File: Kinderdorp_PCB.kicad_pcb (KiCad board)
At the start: 2 copper layers, 99.1 x 99.1 mm, 46 parts, among them Q1 2N7002_C306856, U1 AMS1117-3.3_C347222, U2 ESP32-C3-WROOM-02-N4(4MB)

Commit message: moved board to centre
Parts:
- moved BT1: 29.4 mm to (150.1, 90.6)
- moved D1 29.4 mm to (173.2, 127.0)
- moved G*** 29.4 mm to (169.6, 64.8)
- moved LED5 29.4 mm to (159.4, 56.6)
- moved BUTTON1 29.4 mm to (182.7, 99.9)
- moved C1 29.4 mm to (164.8, 127.5)
- moved C3 29.4 mm to (159.2, 141.4)
- moved F1 29.4 mm to (171.4, 133.2)
- moved GND 29.4 mm to (131.1, 116.0)
- moved LED3 29.4 mm to (102.8, 84.9)
- moved LED4 29.4 mm to (109.8, 57.5)
- moved LED8 29.4 mm to (151.8, 134.5)
- moved LS1 29.4 mm to (122.3, 81.5)
- moved R1 29.4 mm to (104.2, 122.1)
- moved R3 29.4 mm to (178.7, 124.8)
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
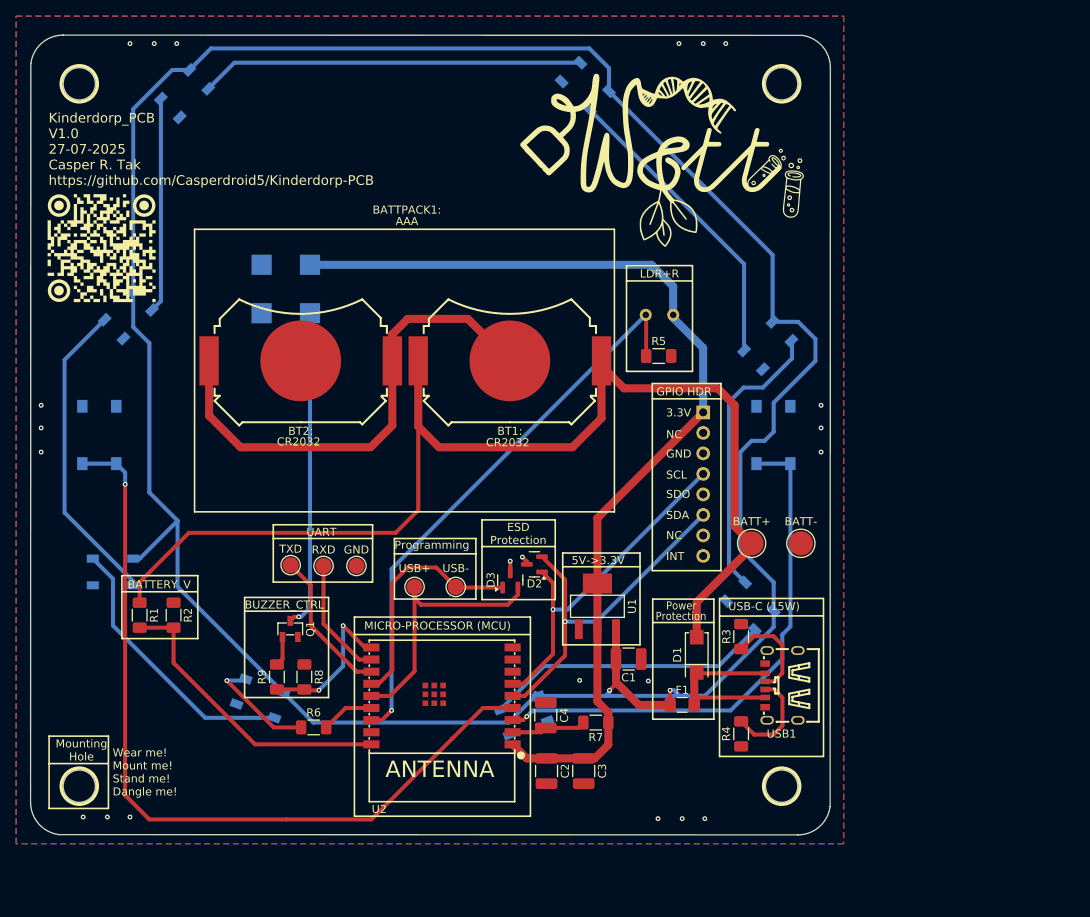
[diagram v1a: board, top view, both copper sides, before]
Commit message: fixed button design error
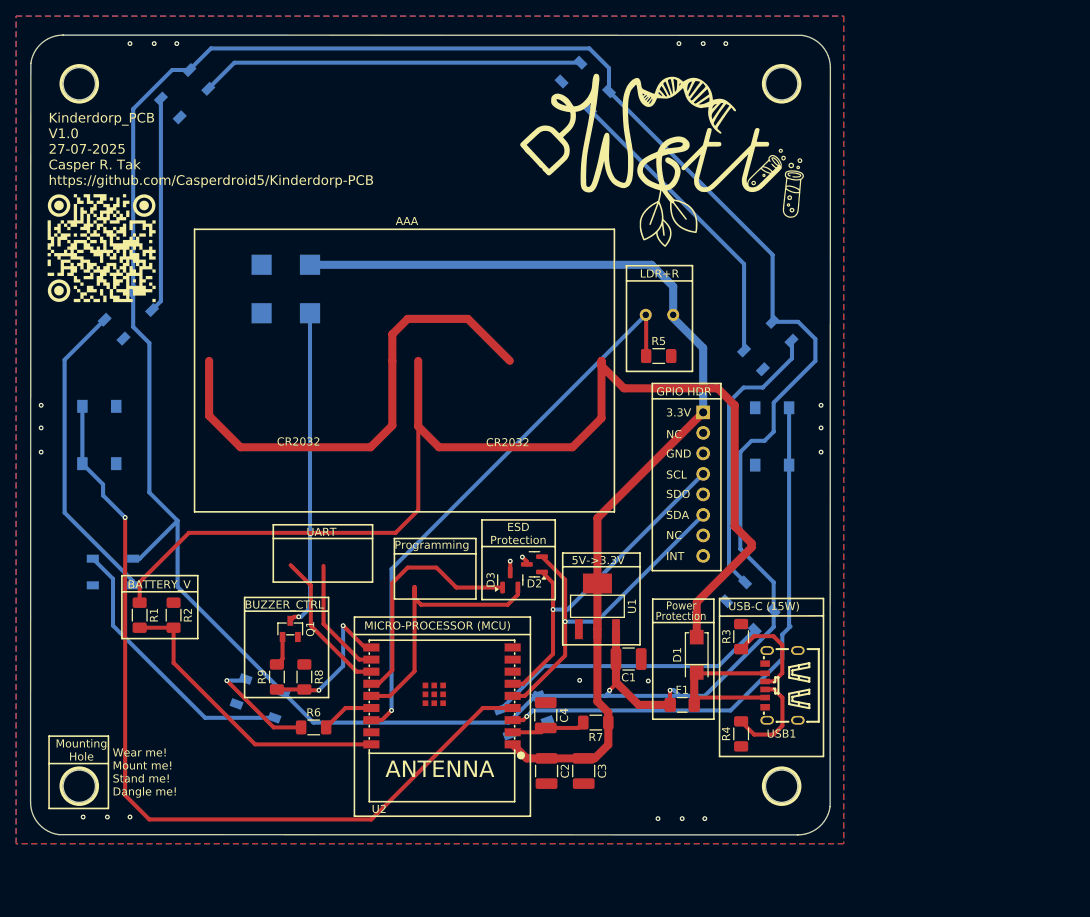
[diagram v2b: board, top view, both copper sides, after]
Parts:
- removed BATT+: ~, TestPoint:TestPoint_Pad_D3.0mm
- removed BATT-: TestPoint_Alt, TestPoint:TestPoint_Pad_D3.0mm
- removed BATTPACK1:: Batteryplaceholder, MountingHole:MountingHole_2.1mm
- removed BT1:, BT2:: MY-2032-12, easyeda2kicad:BAT-SMD_MY-2032-12
- removed GND, RXD, TXD, USB+, USB-: TestPoint_Probe, TestPoint:TestPoint_Pad_D2.0mm
- F1: value Fuse_Small 2A -> Resetable fuse 0.75A
- R9: value 200 -> 100
- turned BUTTON1 to 90 degrees
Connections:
- BUTTON1 pad 1: GND -> GPIO4
- BUTTON1 pad 4: GPIO4 -> GND
- BUTTON2 pad 1: GND -> GPIO5
- BUTTON2 pad 4: GPIO5 -> GND
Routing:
- net GPIO5: track 100.7 -> 105.3 mm
- net GPIO4: track 65.3 -> 68.1 mm

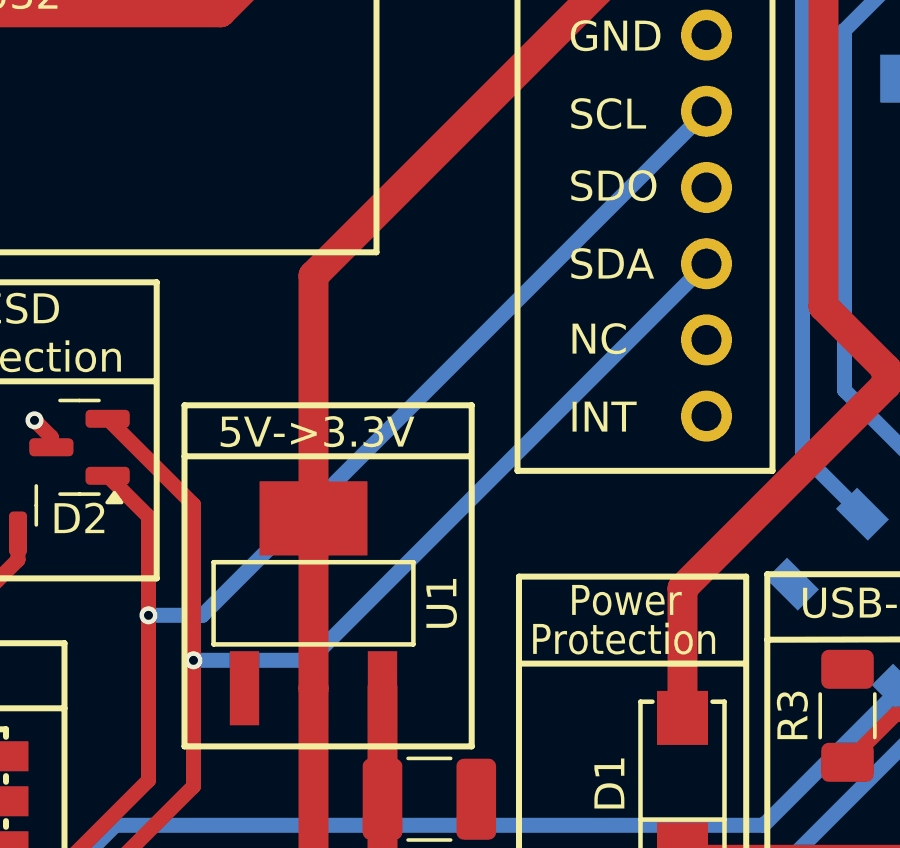
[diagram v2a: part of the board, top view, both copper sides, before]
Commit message: added more lighting effects and updated i2c on pcb (header)
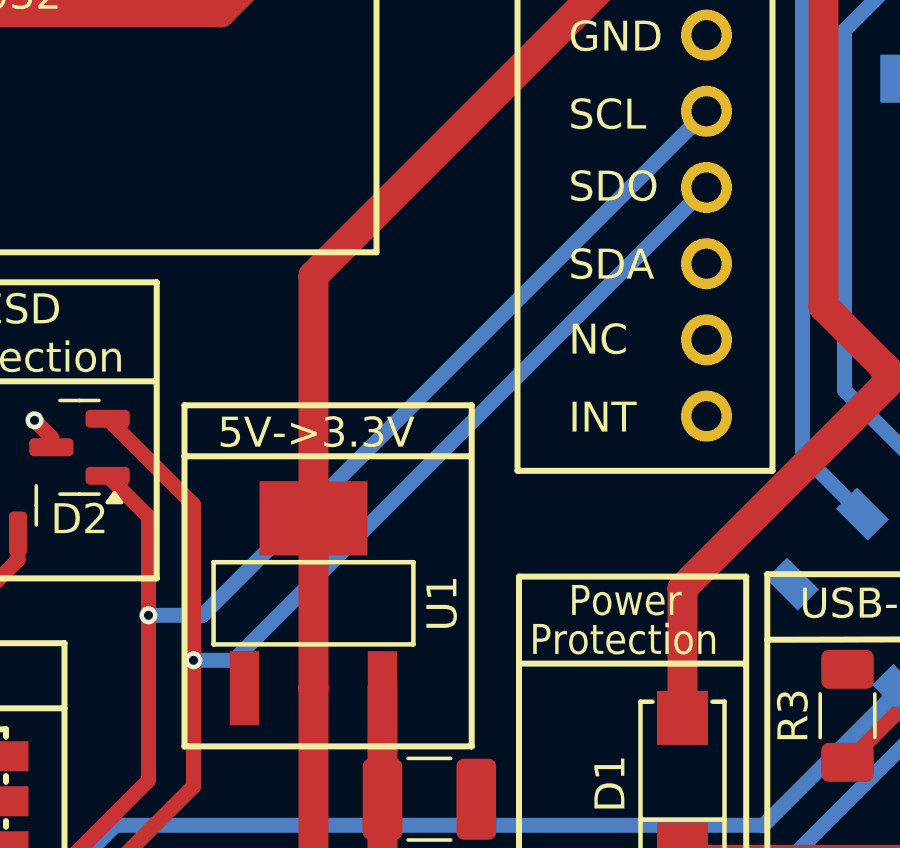
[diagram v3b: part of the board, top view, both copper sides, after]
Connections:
- HDR1 pad 5: SDO -> GPIO6
- HDR1 pad 6: GPIO6 -> unconnected-(HDR1-Pin_6-Pad6)
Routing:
- net GPIO6: track 44.6 -> 45.6 mm
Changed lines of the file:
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@@
 	(net 3 "BUZZ")
 	(net 4 "INT")
-	(net 5 "SDO")
+	(net 5 "unconnected-(HDR1-Pin_6-Pad6)")
 	(net 6 "+5V")
 	(net 7 "Net-(Q1-D)")
@@
 			(layers "*.Cu" "*.Mask")
 			(remove_unused_layers no)
-			(net 5 "SDO")
+			(net 10 "GPIO6")
 			(pinfunction "Pin_5")
 			(pintype "passive")
@@
 			(layers "*.Cu" "*.Mask")
 			(remove_unused_layers no)
-			(net 10 "GPIO6")
+			(net 5 "unconnected-(HDR1-Pin_6-Pad6)")
 			(pinfunction "Pin_6")
-			(pintype "passive")
+			(pintype "passive+no_connect")
 		)
 		(pad "7" thru_hole circle
@@
 	)
 	(segment
-		(start 160.825238 122.9)
-		(end 174.045238 109.68)
+		(start 158.285238 122.9)
+		(end 174.045238 107.14)
 		(width 0.5)
 		(layer "B.Cu")
@@
 	(segment
 		(start 156.945238 122.9)
-		(end 160.825238 122.9)
+		(end 158.285238 122.9)
 		(width 0.5)
 		(layer "B.Cu")

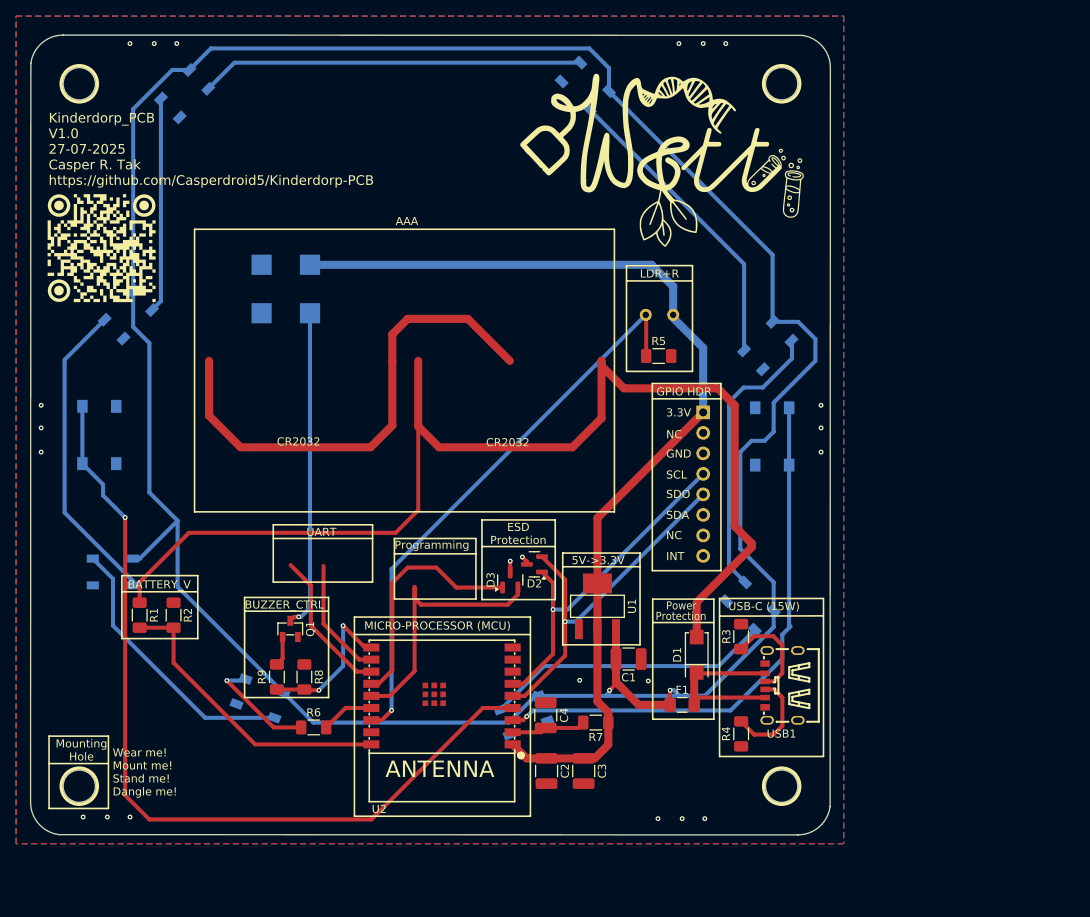
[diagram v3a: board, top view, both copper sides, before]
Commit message: updated PCB to V1.1
removed cr2032 (this is not viable with the current draw of the board)
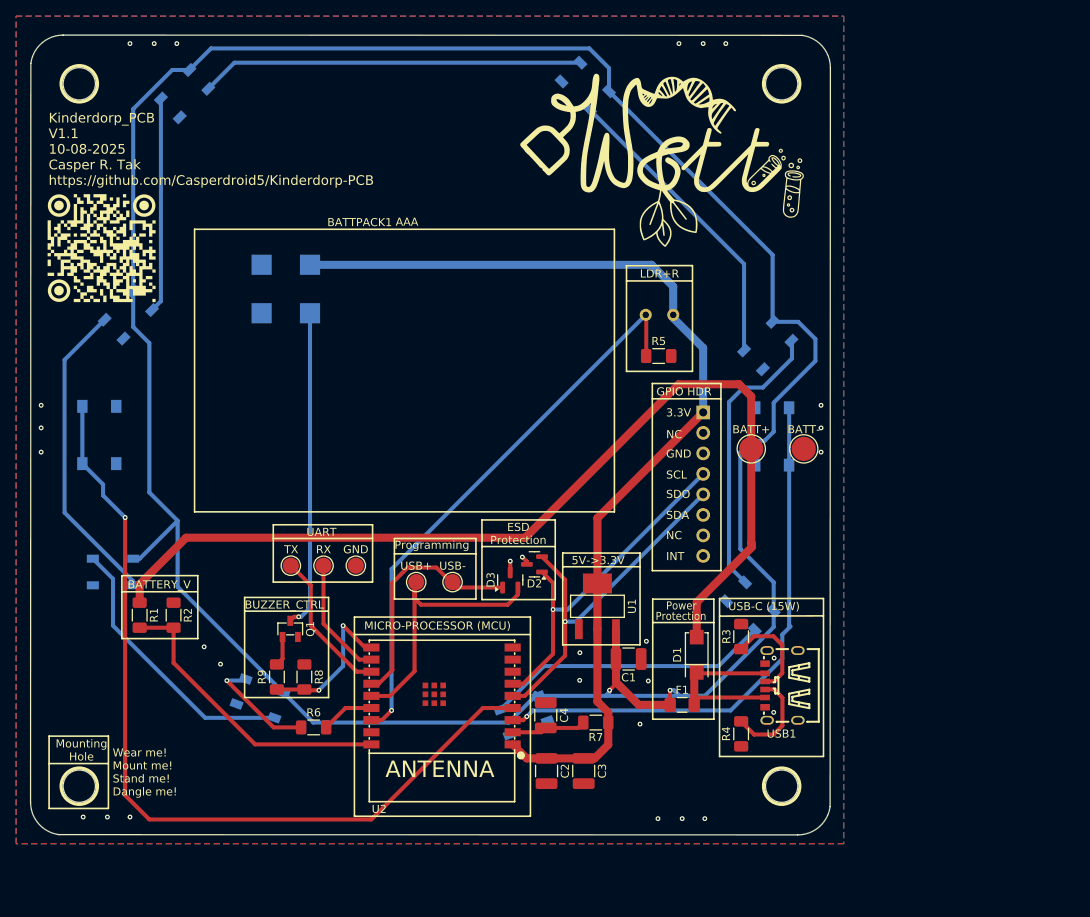
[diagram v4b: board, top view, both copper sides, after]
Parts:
- added BATT+: ~, TestPoint:TestPoint_Pad_D3.0mm, F.Cu at (180.0, 101.5)
- added BATT-: TestPoint_Alt, TestPoint:TestPoint_Pad_D3.0mm, F.Cu at (186.5, 101.5)
- added BATTPACK1: Batteryplaceholder, MountingHole:MountingHole_2.1mm, F.Cu at (111.0, 91.5)
- added GND: TestPoint_Probe, TestPoint:TestPoint_Pad_D2.0mm, F.Cu at (131.0, 116.0)
- added RX: TestPoint_Probe, TestPoint:TestPoint_Pad_D2.0mm, F.Cu at (127.0, 116.0)
- added TX: TestPoint_Probe, TestPoint:TestPoint_Pad_D2.0mm, F.Cu at (123.0, 116.0)
- added USB+: TestPoint_Probe, TestPoint:TestPoint_Pad_D2.0mm, F.Cu at (138.5, 118.0)
- added USB-: TestPoint_Probe, TestPoint:TestPoint_Pad_D2.0mm, F.Cu at (143.0, 118.0)
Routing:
- net Net-(BT1-Pad2): track 61.0 -> 0.00 mm
- net Net-(D1-A): track 151.3 -> 121.6 mm
- net GND: vias 22 -> 29
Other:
- board text added: "Kinderdorp_PCB V1.1 10-08-2025 Casper R. Tak https://github.com/Casperdroid5/Kinderdorp-PCB"
- board text removed: "CR2032"
- board text removed: "Kinderdorp_PCB V1.0 27-07-2025 Casper R. Tak https://github.com/Casperdroid5/Kinderdorp-PCB"
